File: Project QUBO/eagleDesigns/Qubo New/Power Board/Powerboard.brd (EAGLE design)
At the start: 127 x 88.9 mm, 34 parts, among them IC1 PCF8574T, U1 UEI15, U2 TSR2-2450

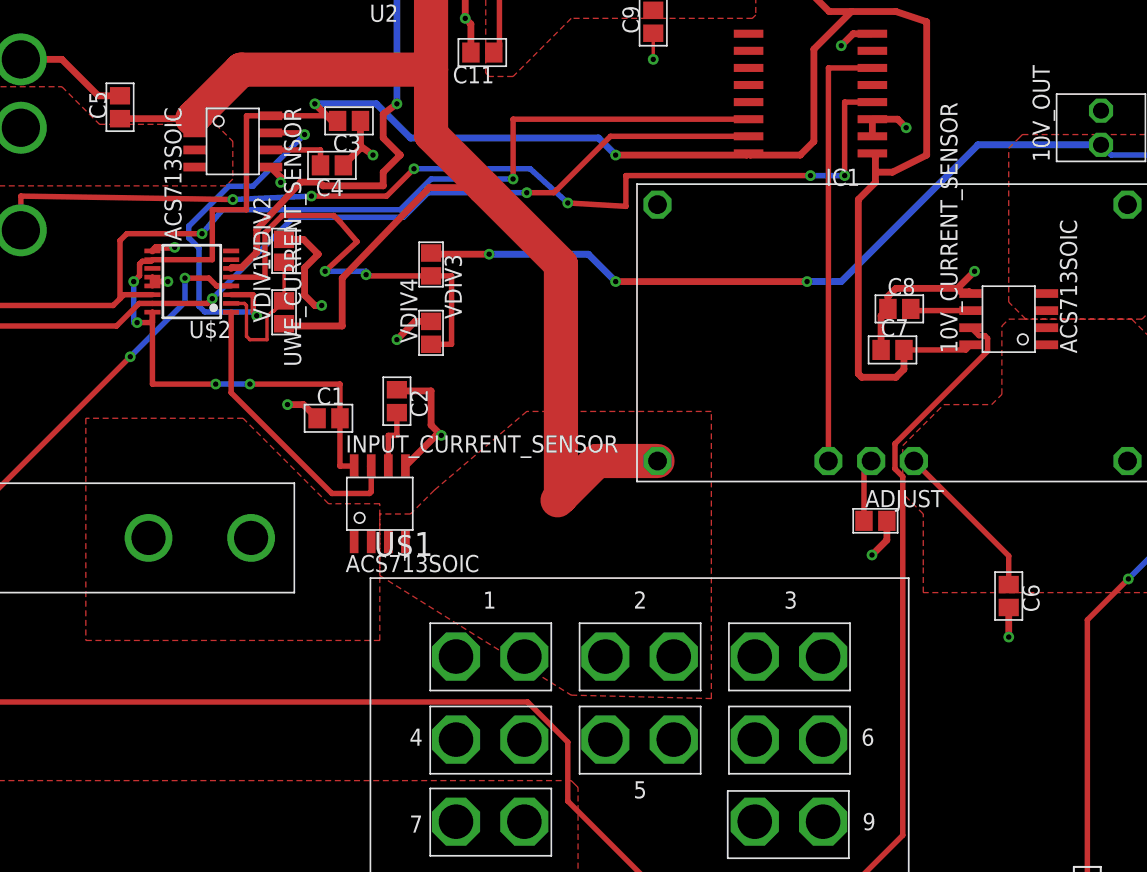
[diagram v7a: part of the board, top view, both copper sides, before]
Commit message: Capacitor and Powerboard
Added capacitor package and adjusted powerboard
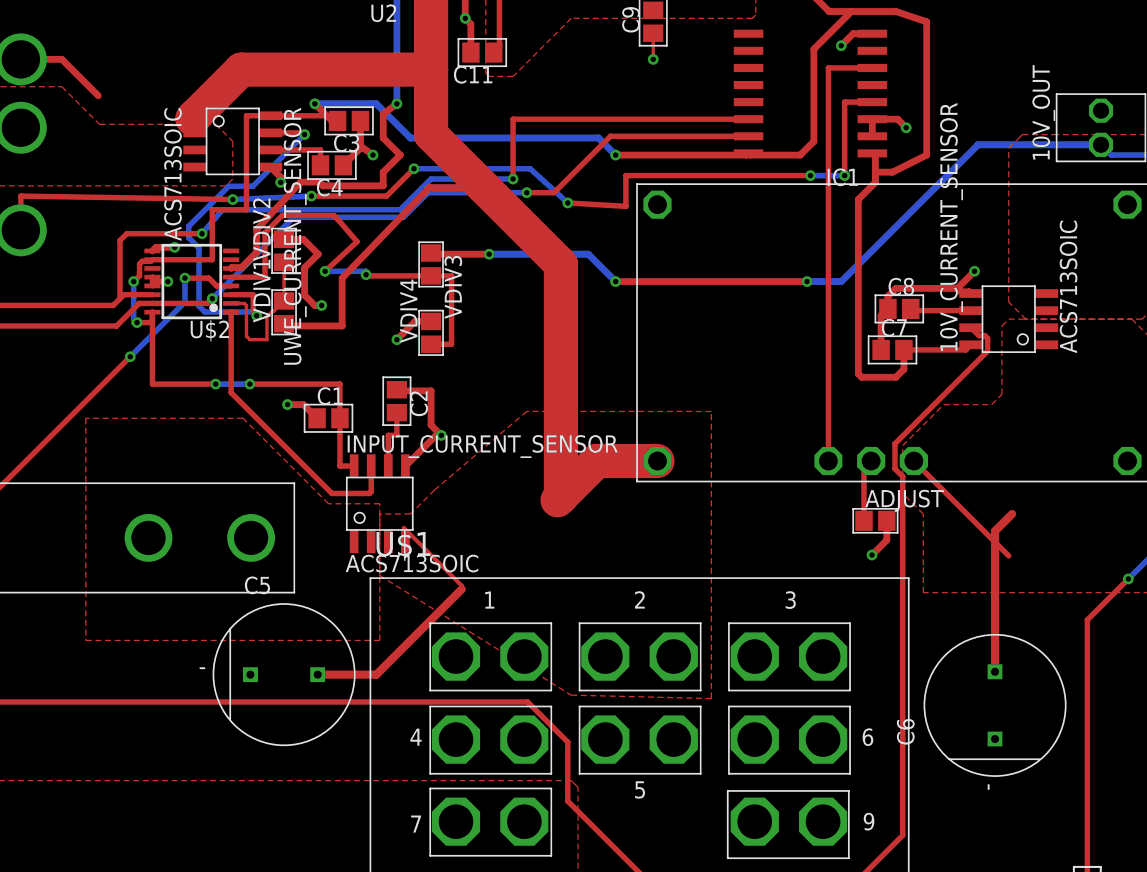
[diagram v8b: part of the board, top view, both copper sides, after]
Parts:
- C5: value XXX -> (none); device resistor:C0805 -> resistor:PANASONIC_A_TYPE_M
- C6: value 330u -> (none); device resistor:C0805 -> resistor:PANASONIC_A_TYPE_M
- moved C5 43.9 mm to (60.2, 26.2), turned to 0 degrees
- moved C6 8.19 mm to (113.0, 23.9), turned to 90 degrees
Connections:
- net 10V_OUT: now also C6.+; no longer C6.1
- net GND: now also C5.-, C6.-; no longer C5.2, C6.2
- net PROCESSED_INPUT: now also C5.+; no longer C5.1
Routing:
- net PROCESSED_INPUT: track 98.7 -> 113.0 mm
- net 10V_OUT: track 12.1 -> 22.2 mm
- net GND: track 89.9 -> 86.1 mm, vias 16 -> 15
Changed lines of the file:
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@@
 <?xml version="1.0" encoding="utf-8"?>
 <!DOCTYPE eagle SYSTEM "eagle.dtd">
-<eagle version="8.6.3">
+<eagle version="8.7.1">
 <drawing>
 <settings>
@@
 <element name="C3" library="resistor" package="C0805" value="0.1u" x="65.024" y="67.31" rot="R180"/>
 <element name="C4" library="resistor" package="C0805" value="47n" x="63.754" y="64.008" rot="R180"/>
-<element name="C5" library="resistor" package="C0805" value="XXX" x="48.006" y="68.326" rot="R90"/>
-<element name="C6" library="resistor" package="C0805" value="330u" x="114.046" y="32.004" rot="R270"/>
 <element name="C7" library="resistor" package="C0805" value="0.1u" x="105.41" y="50.292"/>
 <element name="C8" library="resistor" package="C0805" value="47n" x="105.918" y="53.34"/>
@@
 <element name="U2" library="tracoPower" package="TSR2" value="TSR2-2450" x="73.66" y="80.01"/>
 <element name="C11" library="resistor" package="C0805" value="FILTER" x="74.93" y="72.39" rot="R180"/>
+<element name="C5" library="resistor" package="PANASONIC_A_TYPE_M" value="" x="60.198" y="26.162"/>
+<element name="C6" library="resistor" package="PANASONIC_A_TYPE_M" value="" x="113.03" y="23.876" rot="R90"/>
 </elements>
 <signals>
@@
 <contactref element="VDIV2" pad="2"/>
 <contactref element="10V_REGULATOR" pad="GND1"/>
-<contactref element="C5" pad="2"/>
 <contactref element="10V_REGULATOR" pad="GND2"/>
-<contactref element="C6" pad="2"/>
 <contactref element="ADJUST" pad="2"/>
 <contactref element="C7" pad="1"/>
@@
 <wire x1="104.99" y1="36.156" x2="103.886" y2="35.052" width="0.508" layer="1"/>
 <via x="103.886" y="35.052" extent="1-16" drill="0.4"/>
-<wire x1="114.046" y1="31.154" x2="114.046" y2="28.956" width="0.508" layer="1"/>
-<via x="114.046" y="28.956" extent="1-16" drill="0.4"/>
 <wire x1="97.155" y1="84.588" x2="104.4" y2="84.588" width="0.508" layer="1"/>
 <wire x1="104.4" y1="84.588" x2="106.172" y2="86.36" width="0.508" layer="1"/>
@@
 <wire x1="69.215" y1="41.662" x2="71.495" y2="43.942" width="0.508" layer="1"/>
 <wire x1="71.495" y1="43.942" x2="71.882" y2="43.942" width="0.508" layer="1"/>
-<wire x1="48.006" y1="69.176" x2="46.394" y2="69.176" width="0.508" layer="1"/>
 <wire x1="46.394" y1="69.176" x2="43.688" y2="71.882" width="0.508" layer="1"/>
 <wire x1="43.688" y1="71.882" x2="40.64" y2="71.882" width="0.508" layer="1"/>
@@
 <wire x1="87.63" y1="73.826" x2="87.63" y2="71.882" width="0.254" layer="1"/>
 <via x="87.63" y="71.882" extent="1-16" drill="0.4"/>
+<contactref element="C5" pad="-"/>
+<contactref element="C6" pad="-"/>
 </signal>
 <signal name="N$1">
@@
 <contactref element="VDIV1" pad="1"/>
 <contactref element="10V_REGULATOR" pad="VIN"/>
-<contactref element="C5" pad="1"/>
 <contactref element="U$1" pad="2A"/>
 <contactref element="U$1" pad="2B"/>
@@
 <wire x1="53.588" y1="67.691" x2="57.017" y2="71.12" width="2.54" layer="1"/>
 <wire x1="57.017" y1="71.12" x2="71.12" y2="71.12" width="2.54" layer="1"/>
-<wire x1="48.006" y1="67.476" x2="53.373" y2="67.476" width="0.508" layer="1"/>
 <wire x1="53.373" y1="67.476" x2="53.588" y2="67.691" width="2.54" layer="1"/>
 <wire x1="75.057" y1="62.357" x2="70.993" y2="62.357" width="0.508" layer="1"/>
@@
 <wire x1="64.516" y1="55.626" x2="64.516" y2="52.07" width="0.508" layer="1"/>
 <wire x1="64.516" y1="52.07" x2="60.706" y2="52.07" width="0.508" layer="1"/>
+<contactref element="C5" pad="+"/>
+<wire x1="62.698" y1="26.162" x2="62.738" y2="26.162" width="0.1524" layer="1"/>
+<wire x1="73.406" y1="32.512" x2="73.406" y2="32.766" width="0.3048" layer="1"/>
+<wire x1="73.406" y1="32.766" x2="69.088" y2="37.084" width="0.3048" layer="1"/>
+<wire x1="62.698" y1="26.162" x2="67.056" y2="26.162" width="0.6096" layer="1"/>
+<wire x1="67.056" y1="26.162" x2="73.406" y2="32.512" width="0.6096" layer="1"/>
 <wire x1="53.373" y1="67.476" x2="53.588" y2="66.421" width="0" layer="19" extent="1-1"/>
 <wire x1="60.198" y1="52.236" x2="60.706" y2="52.07" width="0" layer="19" extent="1-1"/>
@@
 <contactref element="10V_REGULATOR" pad="VOUT"/>
 <contactref element="10V_REGULATOR" pad="SENSE"/>
-<contactref element="C6" pad="1"/>
 <contactref element="10V_CURRENT_SENSOR" pad="P$1"/>
 <contactref element="10V_CURRENT_SENSOR" pad="P$2"/>
 <wire x1="106.9975" y1="42.037" x2="114.046" y2="34.9885" width="0.4064" layer="1"/>
-<wire x1="114.046" y1="34.9885" x2="114.046" y2="32.854" width="0.4064" layer="1"/>
 <polygon width="0.4064" layer="1" thermals="no">
 <vertex x="115.062" y="52.578"/>
@@
 <vertex x="114.046" y="52.578"/>
 </polygon>
+<contactref element="C6" pad="+"/>
+<wire x1="113.03" y1="26.376" x2="113.03" y2="36.83" width="0.6096" layer="1"/>
+<wire x1="113.03" y1="36.83" x2="114.3" y2="38.1" width="0.6096" layer="1"/>
 </signal>
 <signal name="N$5">
